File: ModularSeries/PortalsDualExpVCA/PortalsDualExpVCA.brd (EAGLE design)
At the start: 47 x 95 mm, 71 parts, among them IC1 LM13700_DIP, IC2 TL0X4_DIP, IC3 TL0X4_DIP, Q1 2N3906, Q2 2N3906, Q3 2N3906, Q4 2N3906

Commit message: Portals files updated, schematic exports and images included
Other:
- board text added: "Portals Dual Exponential Voltage Controlled Amplifier"
- board text removed: "Dual Exponential Voltage Controlled Amplifier"
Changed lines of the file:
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@@
 <text x="4.7625" y="80.3275" size="1.4224" layer="21" font="vector" ratio="12" align="center">2</text>
 <text x="4.7625" y="82.8675" size="1.4224" layer="21" font="vector" ratio="12" align="center">1</text>
-<text x="23.495" y="90.4875" size="1.4224" layer="21" font="vector" ratio="12" align="center">Dual Exponential
+<text x="23.495" y="90.4875" size="1.4224" layer="21" font="vector" ratio="12" align="center">Portals
+Dual Exponential
 Voltage Controlled Amplifier</text>
 <text x="23.495" y="4.445" size="1.4224" layer="21" font="vector" ratio="12" align="center">v2.0

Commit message: Library updated, variants consolidated
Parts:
- IC1: value LM13700_DIP -> (none)
- IC2, IC3: value TL0X4_DIP -> (none)
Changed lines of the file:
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@@
 <attribute name="POPULARITY" value="7" x="73.58" y="73.49" size="1.778" layer="27" display="off"/>
 </element>
-<element name="IC1" library="ElectricNoodleBox" package="DIL16" package3d_urn="urn:adsk.eagle:package:922/2" value="LM13700_DIP" x="22.86" y="47.49" smashed="yes">
+<element name="IC1" library="ElectricNoodleBox" package="DIL16" package3d_urn="urn:adsk.eagle:package:922/2" value="" x="22.86" y="47.49" smashed="yes">
 <attribute name="NAME" x="12.065" y="47.49" size="1.016" layer="25" font="vector" ratio="20" rot="R90" align="bottom-center"/>
 <attribute name="VALUE" x="34.29" y="47.49" size="0.6096" layer="27" font="vector" ratio="20" rot="R90" align="bottom-center"/>
 </element>
-<element name="IC2" library="ElectricNoodleBox" package="DIL14" package3d_urn="urn:adsk.eagle:package:16407/2" value="TL0X4_DIP" x="25.4" y="19.55" smashed="yes" rot="R270">
+<element name="IC2" library="ElectricNoodleBox" package="DIL14" package3d_urn="urn:adsk.eagle:package:16407/2" value="" x="25.4" y="19.55" smashed="yes" rot="R270">
 <attribute name="NAME" x="22.352" y="28.821" size="1.27" layer="25" ratio="10"/>
 <attribute name="VALUE" x="24.765" y="26.281" size="1.27" layer="27" ratio="10" rot="R270"/>
 </element>
-<element name="IC3" library="ElectricNoodleBox" package="DIL14" package3d_urn="urn:adsk.eagle:package:16407/2" value="TL0X4_DIP" x="25.4" y="75.43" smashed="yes" rot="R270">
+<element name="IC3" library="ElectricNoodleBox" package="DIL14" package3d_urn="urn:adsk.eagle:package:16407/2" value="" x="25.4" y="75.43" smashed="yes" rot="R270">
 <attribute name="NAME" x="22.352" y="84.701" size="1.27" layer="25" ratio="10"/>
 <attribute name="VALUE" x="24.765" y="82.161" size="1.27" layer="27" ratio="10" rot="R270"/>

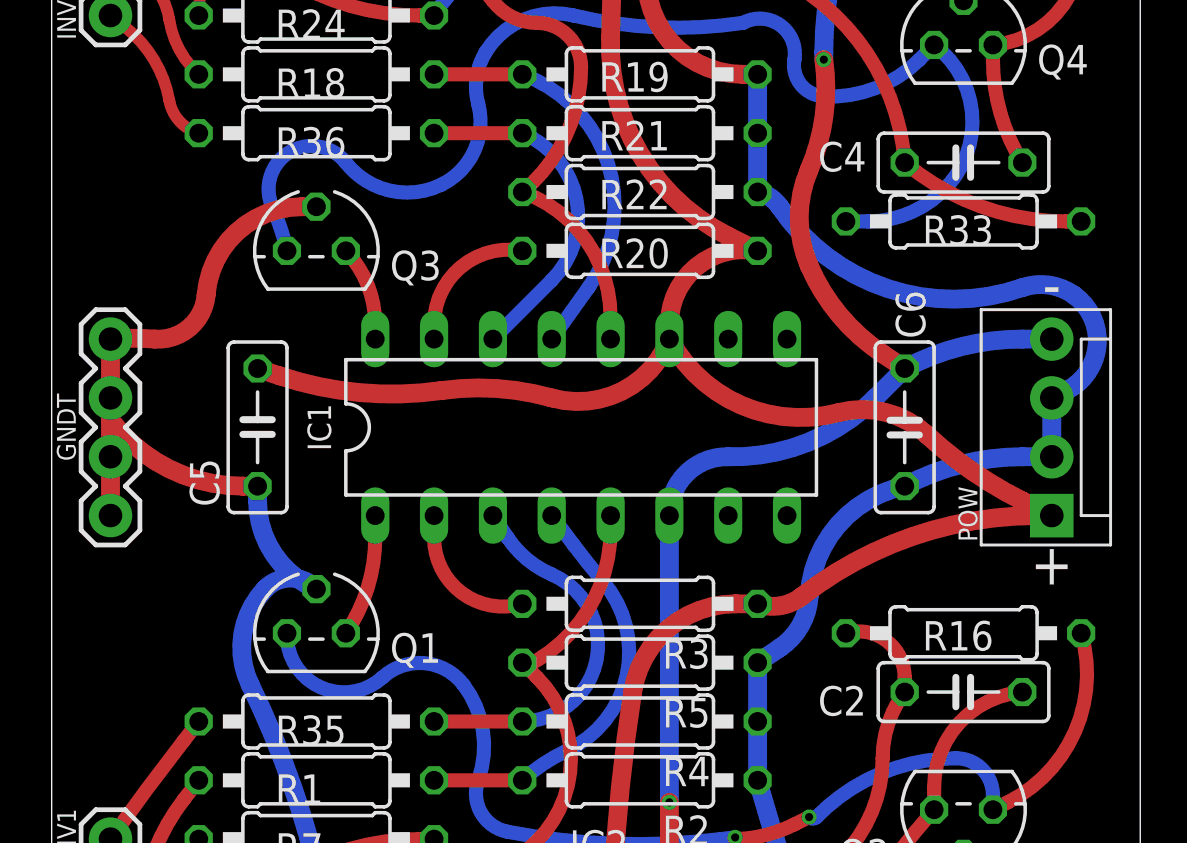
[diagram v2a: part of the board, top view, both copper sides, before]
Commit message: Power header updated on most PCBs. Knives layout added
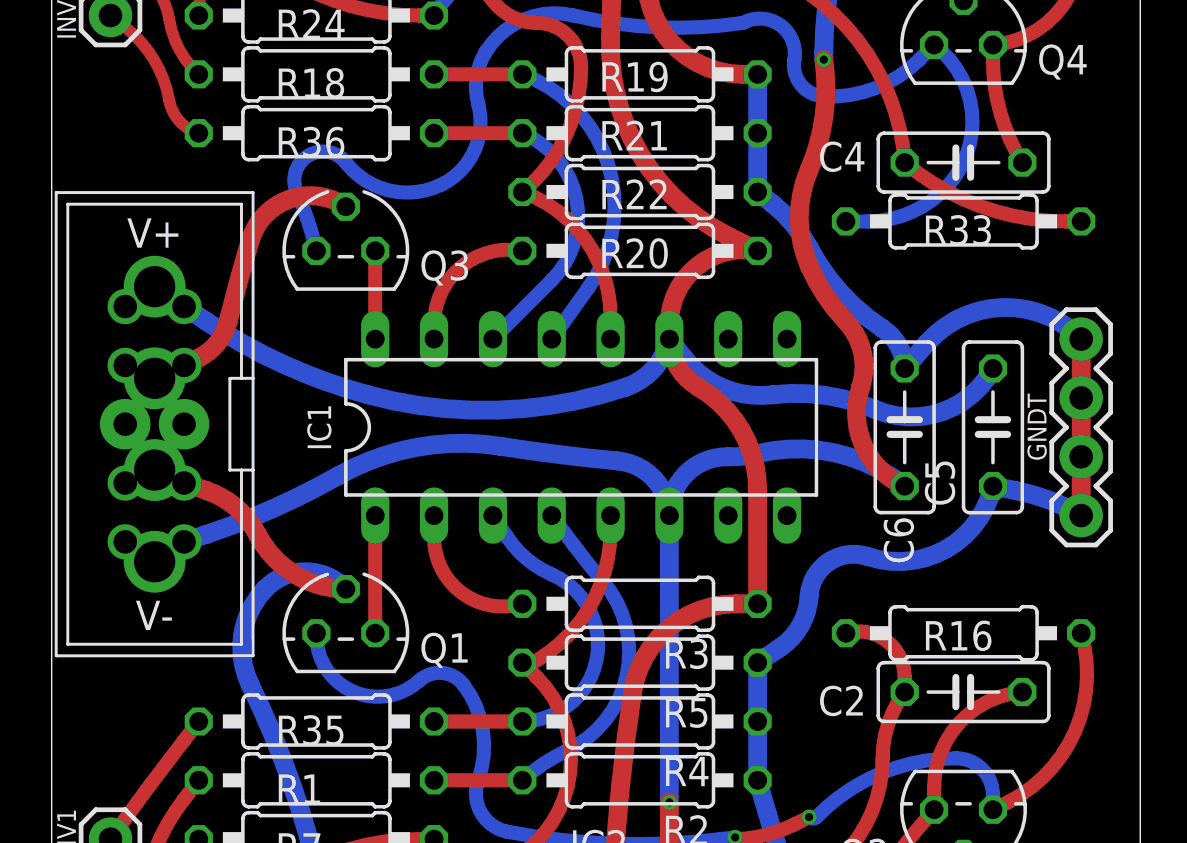
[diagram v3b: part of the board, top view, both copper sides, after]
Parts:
- removed POW: 4XMOLEX, ElectricNoodleBox:MOLEX-1X4
- added WP1: COMBO_SUPPLY_HEADER, ElectricNoodleBox:COMBINED_POWER
- moved GNDT 41.9 mm to (44.5, 43.7)
- moved C5 31.8 mm to (40.6, 47.5)
- moved Q1 1.27 mm to (12.7, 38.6)
- moved Q3 1.27 mm to (12.7, 55.1)
- turned C6 to 90 degrees
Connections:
- net +12V: now also WP1.V+1, WP1.V+2, WP1.V+3; no longer POW.1
- net -12V: now also WP1.V-1, WP1.V-2, WP1.V-3; no longer POW.4
- net AGND: now also WP1.GND1, WP1.GND2, WP1.GND3, WP1.GND4, WP1.GND5, WP1.GND6, WP1.GND7, WP1.GND8; no longer POW.2, POW.3
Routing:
- net -12V: track 163.7 -> 183.4 mm
- net AGND: track 252.1 -> 246.0 mm
- net N$17: track 46.4 -> 45.2 mm
- net N$37: track 48.4 -> 47.8 mm
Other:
- board text removed: "+"
- board text removed: "-"

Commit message: Control PCBs for Prism, Portals, TimeSeeds and Knives added
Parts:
- R14, R31: value 470Ω -> 100Ω
- R17, R26, R34, R9: value 100K -> 75K
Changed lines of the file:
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@@
 <attribute name="VALUE" x="34.87" y="10.52" size="1.27" layer="27"/>
 </element>
-<element name="R14" library="rcl" library_urn="urn:adsk.eagle:library:334" package="0207/10" package3d_urn="urn:adsk.eagle:package:23491/2" value="470Ω" x="39.37" y="10.66" smashed="yes">
+<element name="R14" library="rcl" library_urn="urn:adsk.eagle:library:334" package="0207/10" package3d_urn="urn:adsk.eagle:package:23491/2" value="100Ω" x="39.37" y="10.66" smashed="yes">
 <attribute name="NAME" x="37.592" y="9.644" size="1.27" layer="25" ratio="10"/>
 <attribute name="POPULARITY" value="81" x="71.12" y="-37.6" size="1.778" layer="27" display="off"/>
@@
 <attribute name="VALUE" x="41.6306" y="39.235" size="1.27" layer="27" ratio="10" rot="R180"/>
 </element>
-<element name="R17" library="rcl" library_urn="urn:adsk.eagle:library:334" package="0207/10" package3d_urn="urn:adsk.eagle:package:23491/2" value="100K" x="11.43" y="19.55" smashed="yes">
+<element name="R17" library="rcl" library_urn="urn:adsk.eagle:library:334" package="0207/10" package3d_urn="urn:adsk.eagle:package:23491/2" value="75K" x="11.43" y="19.55" smashed="yes">
 <attribute name="NAME" x="9.652" y="18.534" size="1.27" layer="25" ratio="10"/>
 <attribute name="POPULARITY" value="81" x="81.28" y="-28.71" size="1.778" layer="27" display="off"/>
@@
 <attribute name="VALUE" x="9.1694" y="79.875" size="1.27" layer="27" ratio="10"/>
 </element>
-<element name="R26" library="rcl" library_urn="urn:adsk.eagle:library:334" package="0207/10" package3d_urn="urn:adsk.eagle:package:23491/2" value="100K" x="11.43" y="77.97" smashed="yes">
+<element name="R26" library="rcl" library_urn="urn:adsk.eagle:library:334" package="0207/10" package3d_urn="urn:adsk.eagle:package:23491/2" value="75K" x="11.43" y="77.97" smashed="yes">
 <attribute name="NAME" x="9.652" y="76.954" size="1.27" layer="25" ratio="10"/>
 <attribute name="POPULARITY" value="81" x="68.58" y="19.55" size="1.778" layer="27" display="off"/>
@@
 <attribute name="VALUE" x="34.87" y="76.56" size="1.27" layer="27"/>
 </element>
-<element name="R31" library="rcl" library_urn="urn:adsk.eagle:library:334" package="0207/10" package3d_urn="urn:adsk.eagle:package:23491/2" value="470Ω" x="39.37" y="84.32" smashed="yes">
+<element name="R31" library="rcl" library_urn="urn:adsk.eagle:library:334" package="0207/10" package3d_urn="urn:adsk.eagle:package:23491/2" value="100Ω" x="39.37" y="84.32" smashed="yes">
 <attribute name="NAME" x="37.592" y="83.304" size="1.27" layer="25" ratio="10"/>
 <attribute name="POPULARITY" value="81" x="83.82" y="20.82" size="1.778" layer="27" display="off"/>
@@
 <attribute name="VALUE" x="37.1094" y="55.745" size="1.27" layer="27" ratio="10"/>
 </element>
-<element name="R34" library="rcl" library_urn="urn:adsk.eagle:library:334" package="0207/10" package3d_urn="urn:adsk.eagle:package:23491/2" value="100K" x="11.43" y="75.43" smashed="yes">
+<element name="R34" library="rcl" library_urn="urn:adsk.eagle:library:334" package="0207/10" package3d_urn="urn:adsk.eagle:package:23491/2" value="75K" x="11.43" y="75.43" smashed="yes">
 <attribute name="NAME" x="9.652" y="74.414" size="1.27" layer="25" ratio="10"/>
 <attribute name="POPULARITY" value="81" x="30.48" y="6.85" size="1.778" layer="27" display="off"/>
@@
 <attribute name="VALUE" x="9.1694" y="13.835" size="1.27" layer="27" ratio="10"/>
 </element>
-<element name="R9" library="rcl" library_urn="urn:adsk.eagle:library:334" package="0207/10" package3d_urn="urn:adsk.eagle:package:23491/2" value="100K" x="11.43" y="17.01" smashed="yes">
+<element name="R9" library="rcl" library_urn="urn:adsk.eagle:library:334" package="0207/10" package3d_urn="urn:adsk.eagle:package:23491/2" value="75K" x="11.43" y="17.01" smashed="yes">
 <attribute name="NAME" x="9.652" y="15.994" size="1.27" layer="25" ratio="10"/>
 <attribute name="POPULARITY" value="81" x="55.88" y="-26.17" size="1.778" layer="27" display="off"/>

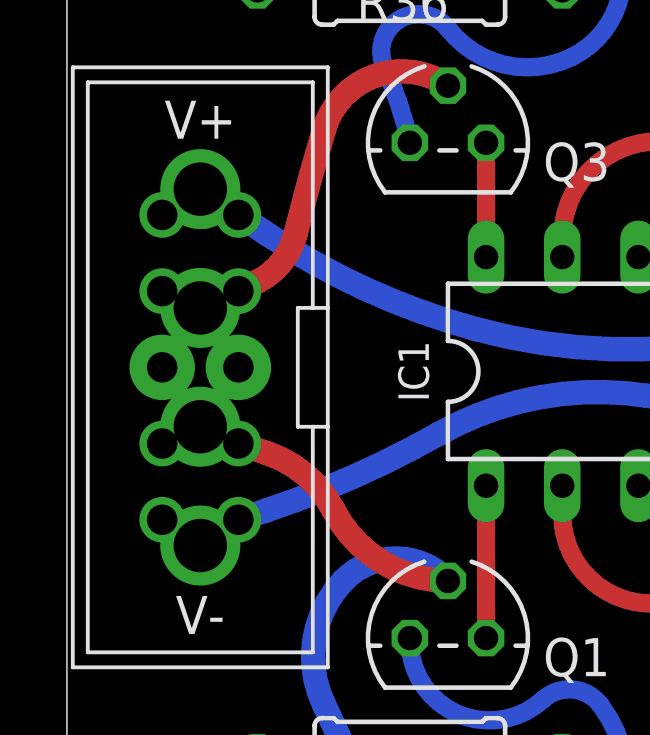
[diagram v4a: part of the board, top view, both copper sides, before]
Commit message: DRC check fixes on Prism, Portals, TimeSeeds and Knives
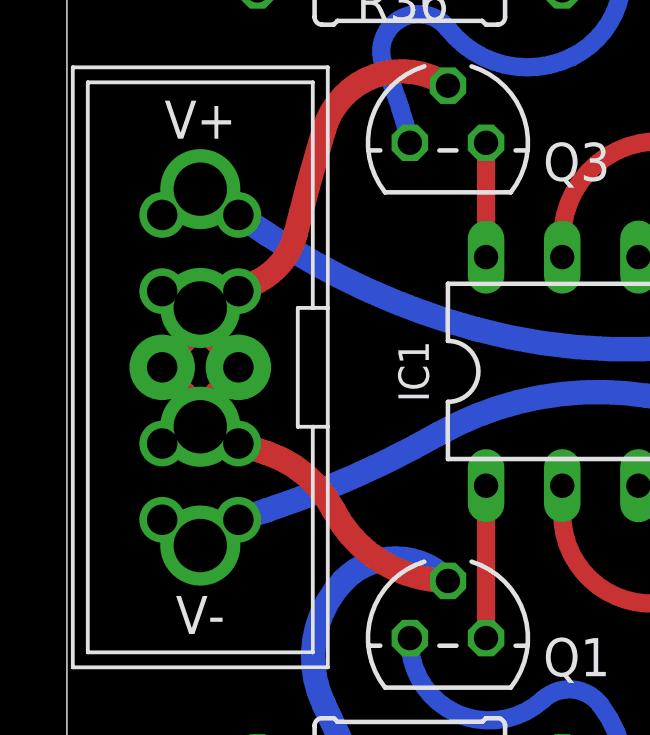
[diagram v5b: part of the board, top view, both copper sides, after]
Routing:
- net AGND: track 246.0 -> 260.6 mm
- net -12V: track 183.4 -> 186.7 mm
- net +12V: track 147.7 -> 150.9 mm
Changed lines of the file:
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@@
 <wire x1="36.83" y1="50.03" x2="37.7825" y2="51.1175" width="0.8128" layer="16"/>
 <wire x1="37.7825" y1="51.1175" x2="44.45" y2="51.3" width="0.8128" layer="16" curve="-94.43648"/>
-<wire x1="4.445" y1="49.605" x2="5.715" y2="50.165" width="0" layer="19" extent="1-1"/>
-<wire x1="3.175" y1="50.165" x2="4.445" y2="49.605" width="0" layer="19" extent="1-1"/>
-<wire x1="5.715" y1="47.625" x2="4.445" y2="49.605" width="0" layer="19" extent="1-1"/>
-<wire x1="3.175" y1="47.625" x2="4.445" y2="49.605" width="0" layer="19" extent="1-1"/>
-<wire x1="4.445" y1="45.645" x2="5.715" y2="47.625" width="0" layer="19" extent="1-1"/>
-<wire x1="3.175" y1="45.085" x2="4.445" y2="45.645" width="0" layer="19" extent="1-1"/>
-<wire x1="5.715" y1="45.085" x2="4.445" y2="45.645" width="0" layer="19" extent="1-1"/>
+<wire x1="4.445" y1="49.605" x2="3.735" y2="49.605" width="0.6096" layer="1"/>
+<wire x1="3.735" y1="49.605" x2="3.175" y2="50.165" width="0.6096" layer="1"/>
+<wire x1="4.445" y1="49.605" x2="5.005" y2="50.165" width="0.6096" layer="1"/>
+<wire x1="5.005" y1="50.165" x2="5.715" y2="50.165" width="0.6096" layer="1"/>
+<wire x1="4.445" y1="45.645" x2="3.885" y2="45.085" width="0.6096" layer="1"/>
+<wire x1="3.885" y1="45.085" x2="3.175" y2="45.085" width="0.6096" layer="1"/>
+<wire x1="4.445" y1="45.645" x2="5.155" y2="45.645" width="0.6096" layer="1"/>
+<wire x1="5.155" y1="45.645" x2="5.715" y2="45.085" width="0.6096" layer="1"/>
+<wire x1="4.445" y1="46.355" x2="5.715" y2="47.625" width="0.6096" layer="1"/>
+<wire x1="4.445" y1="45.645" x2="4.445" y2="46.355" width="0.6096" layer="1"/>
+<wire x1="4.445" y1="46.355" x2="3.175" y2="47.625" width="0.6096" layer="1"/>
+<wire x1="4.445" y1="48.895" x2="3.175" y2="47.625" width="0.6096" layer="1"/>
+<wire x1="4.445" y1="49.605" x2="4.445" y2="48.895" width="0.6096" layer="1"/>
+<wire x1="4.445" y1="48.895" x2="5.715" y2="47.625" width="0.6096" layer="1"/>
 </signal>
 <signal name="N$5">
@@
 <wire x1="30.48" y1="44.7675" x2="27.94" y2="49.2125" width="0.8128" layer="1" curve="59.489763"/>
 <wire x1="27.94" y1="49.2125" x2="26.67" y2="51.3" width="0.8128" layer="1" curve="-56.348262"/>
-<wire x1="3.175" y1="52.705" x2="4.445" y2="53.565" width="0" layer="19" extent="1-1"/>
-<wire x1="5.715" y1="52.705" x2="4.445" y2="53.565" width="0" layer="19" extent="1-1"/>
+<wire x1="3.175" y1="52.705" x2="4.035" y2="53.565" width="0.6096" layer="1"/>
+<wire x1="4.035" y1="53.565" x2="4.445" y2="53.565" width="0.6096" layer="1"/>
+<wire x1="4.445" y1="53.565" x2="4.855" y2="53.565" width="0.6096" layer="1"/>
+<wire x1="4.855" y1="53.565" x2="5.715" y2="52.705" width="0.6096" layer="1"/>
 </signal>
 <signal name="N$7">
@@
 <wire x1="34.29" y1="52.07" x2="34.925" y2="49.2125" width="0.8128" layer="1" curve="-62.052463"/>
 <wire x1="34.925" y1="49.2125" x2="36.83" y2="44.95" width="0.8128" layer="1" curve="85.156551"/>
-<wire x1="4.445" y1="41.685" x2="3.175" y2="42.545" width="0" layer="19" extent="1-1"/>
-<wire x1="5.715" y1="42.545" x2="4.445" y2="41.685" width="0" layer="19" extent="1-1"/>
+<wire x1="4.445" y1="41.685" x2="4.035" y2="41.685" width="0.6096" layer="1"/>
+<wire x1="4.035" y1="41.685" x2="3.175" y2="42.545" width="0.6096" layer="1"/>
+<wire x1="4.445" y1="41.685" x2="5.305" y2="42.545" width="0.6096" layer="1"/>
+<wire x1="5.305" y1="42.545" x2="5.715" y2="42.545" width="0.6096" layer="1"/>
 </signal>
 <signal name="N$18">
@@
 <mfgpreviewcolor name="substratecolor" color="0xFF786E46"/>
 </mfgpreviewcolors>
+<errors>
+</errors>
 </board>
 </drawing>

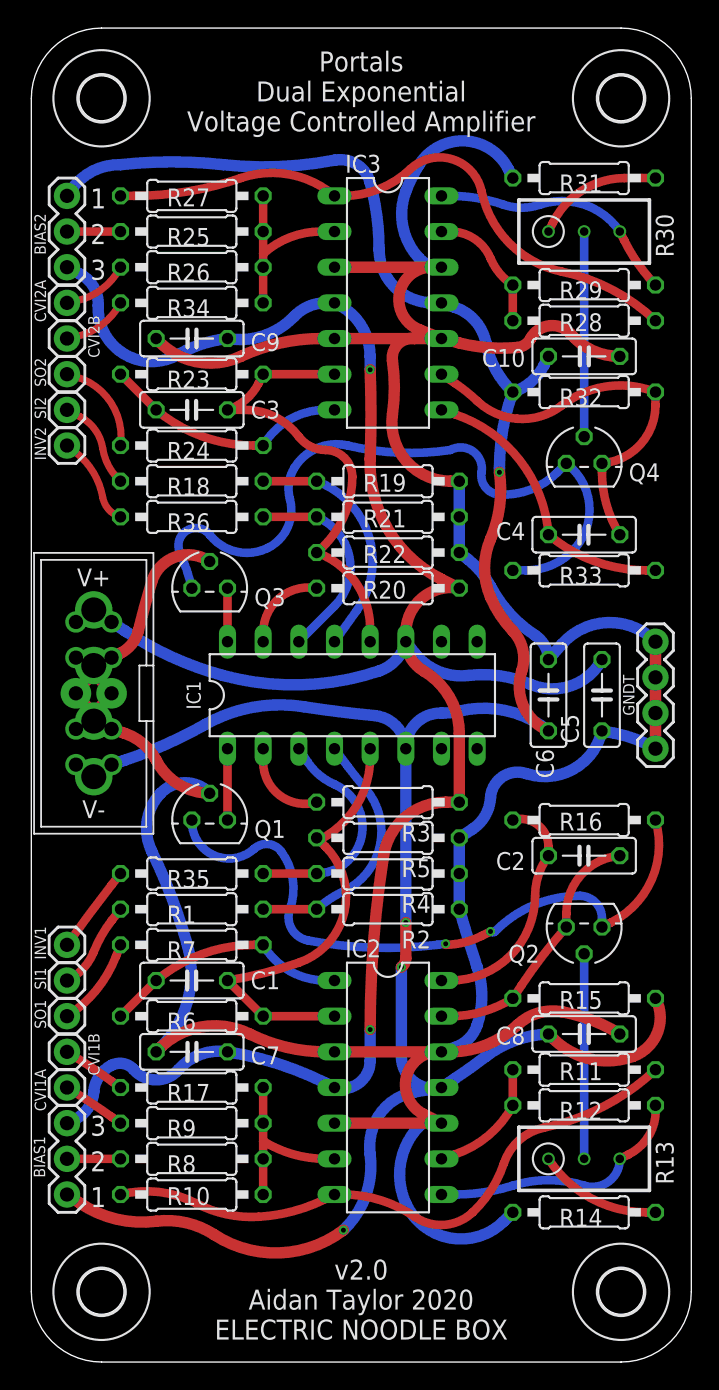
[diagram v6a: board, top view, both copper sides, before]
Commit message: Schematic and Layout fixes to Knives, TimeSeed and Portals
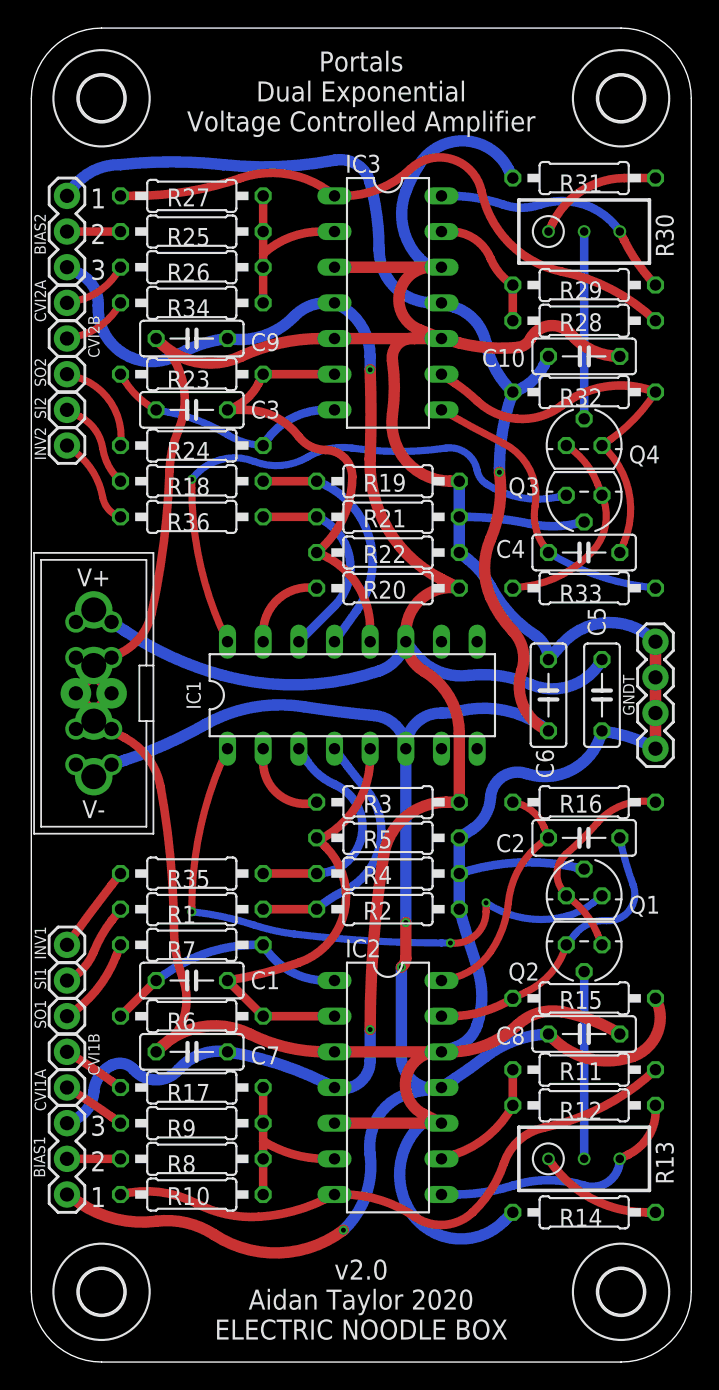
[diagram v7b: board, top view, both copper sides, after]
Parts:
- moved Q3 27.5 mm to (39.4, 61.7), turned to 180 degrees
- moved Q1 27.2 mm to (39.4, 33.2)
- moved C4 1.27 mm to (39.4, 57.6)
- moved R33 1.27 mm to (39.4, 55.1)
- moved Q2 1.27 mm to (39.4, 29.7)
- moved C2 1.27 mm to (39.4, 37.3)
- moved Q4 1.27 mm to (39.4, 65.3)
- moved R16 1.27 mm to (39.4, 39.9)
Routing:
- net N$20: track 5.08 -> 43.2 mm, vias 0 -> 3
- net N$38: track 3.81 -> 39.9 mm, vias 0 -> 1
- net N$37: track 47.8 -> 14.7 mm
- net N$17: track 45.2 -> 15.0 mm, vias 2 -> 0
- net AGND: track 260.6 -> 286.9 mm
- net N$16: track 18.2 -> 20.8 mm
- net N$36: track 19.9 -> 21.6 mm
- net N$35: track 28.2 -> 29.6 mm
- net N$15: track 14.6 -> 13.3 mm
- net N$39: track 14.6 -> 13.3 mm
- net N$18: track 16.0 -> 16.9 mm
